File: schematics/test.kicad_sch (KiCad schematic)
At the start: 9 parts, among them J1 Conn_01x03_Pin, J3 Conn_01x03_Pin, J4 GY-91 MPU6500 + BMP280, Q1 2N2222

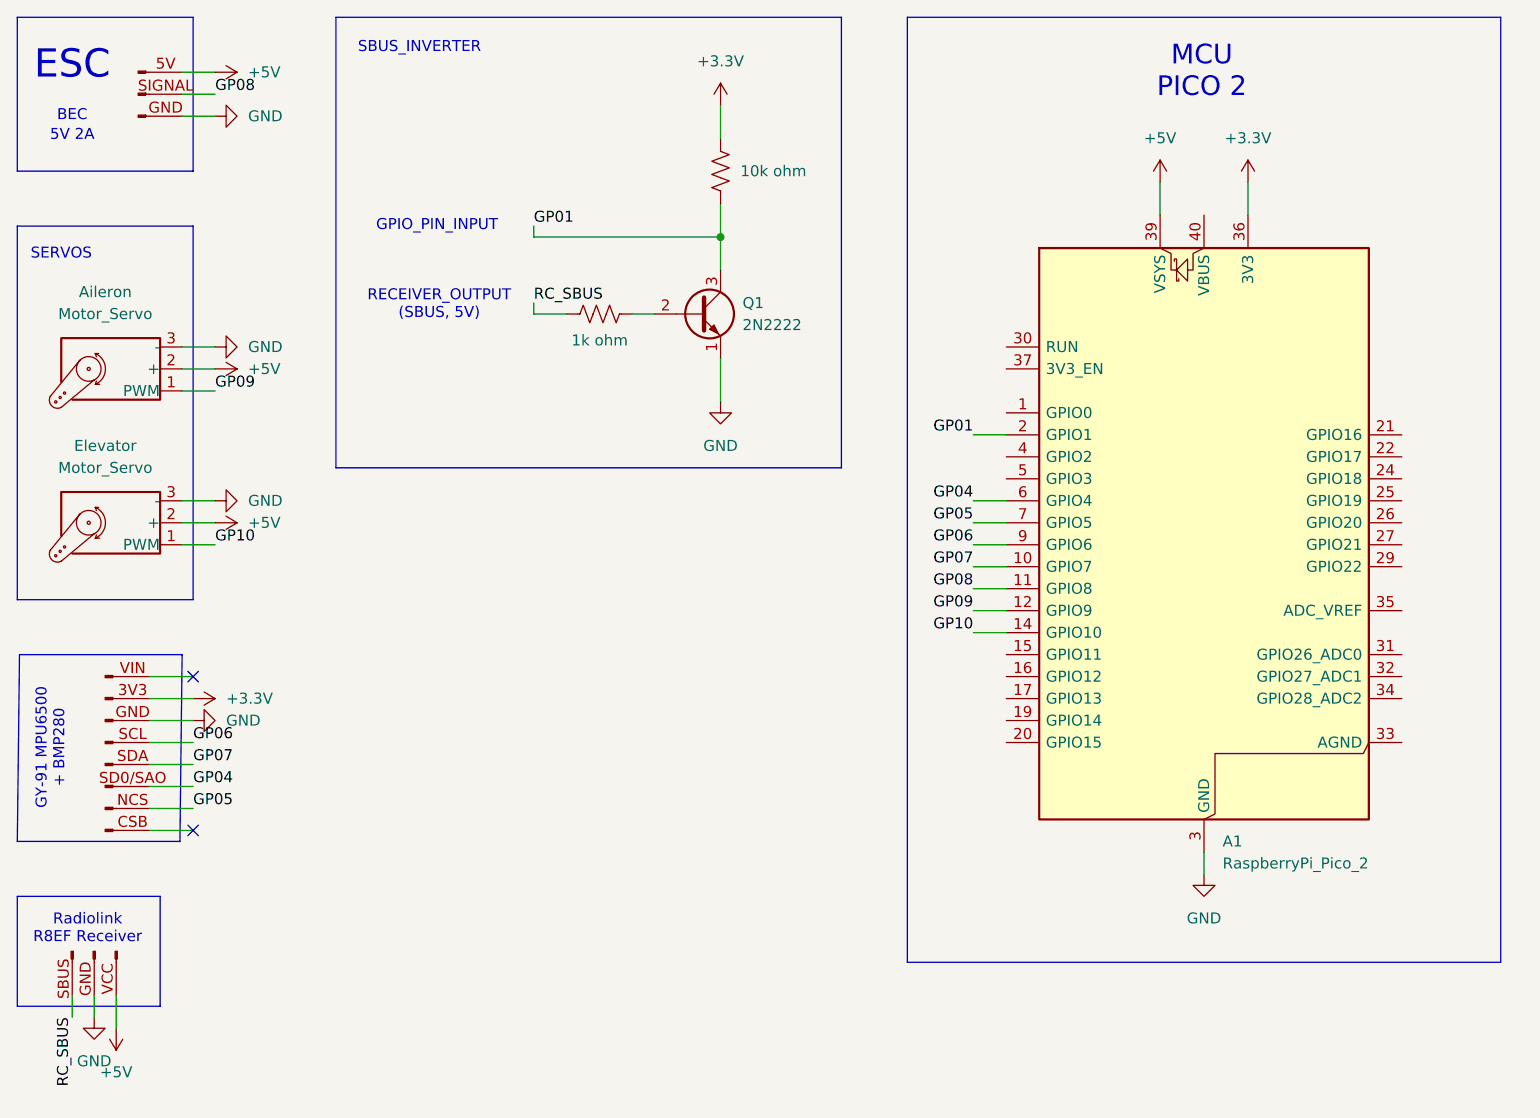
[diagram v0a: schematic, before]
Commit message: schematic, bom updates
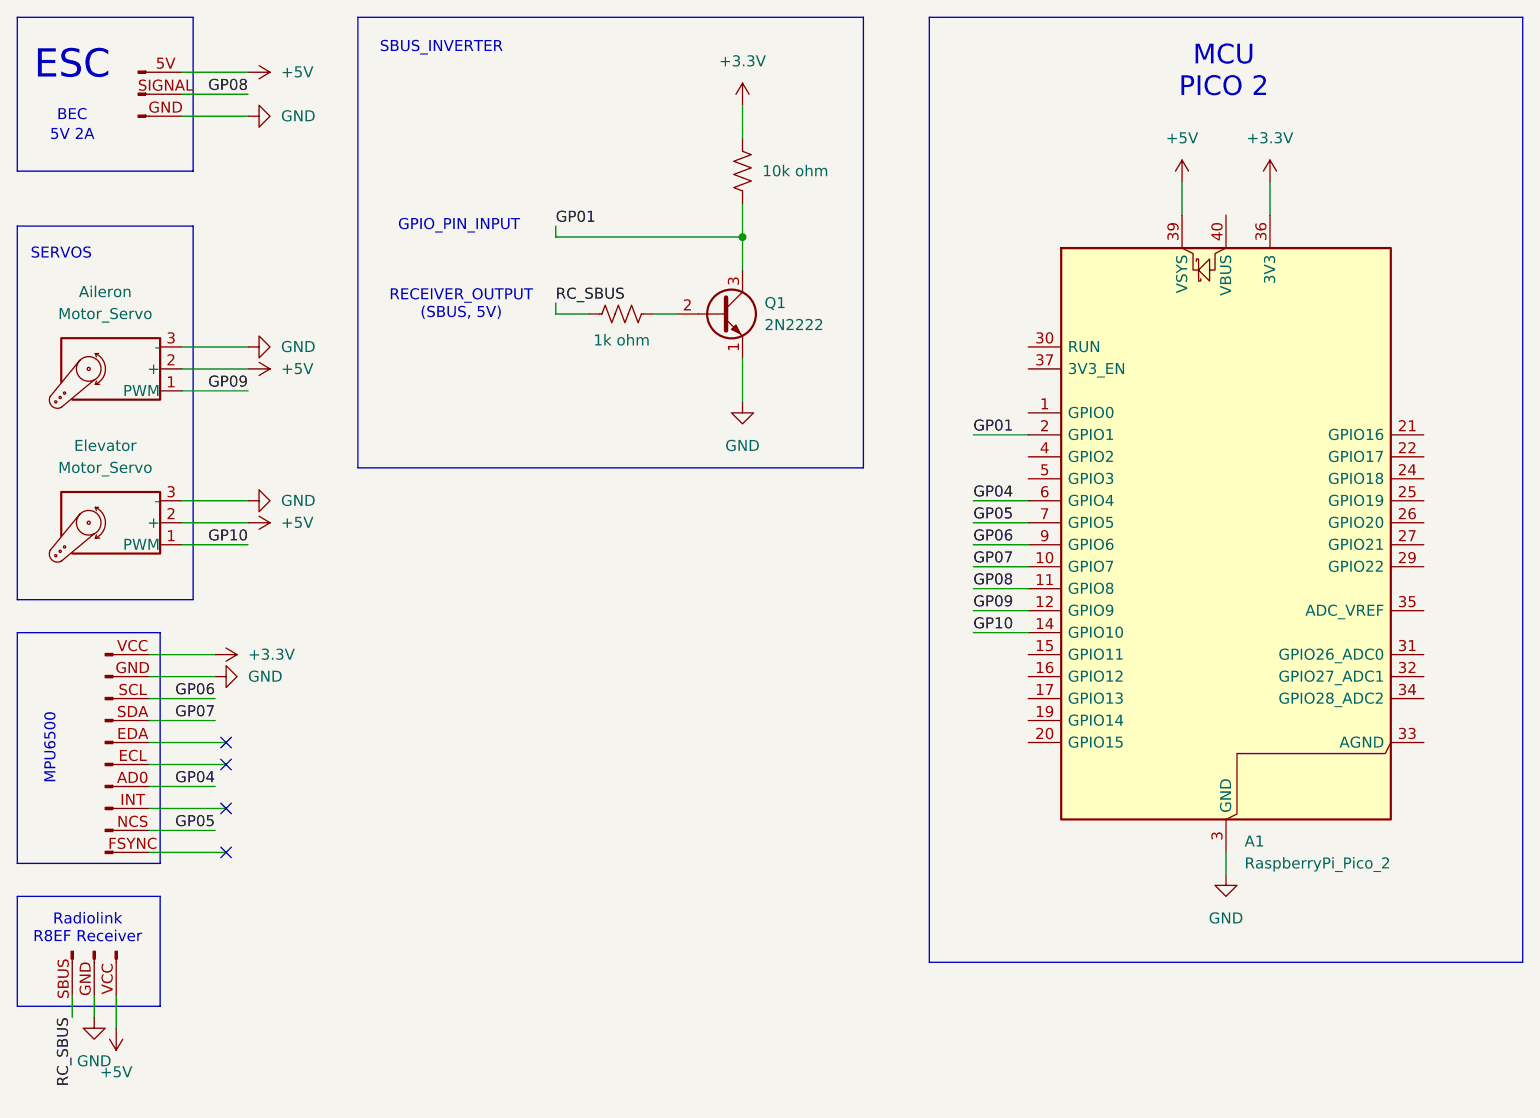
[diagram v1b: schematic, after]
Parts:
- J4: symbol Connector:Conn_01x08_Pin -> Connector:Conn_01x10_Pin
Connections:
- net +3.3V: now also J4.VCC (Pin_1); no longer J4.3V3 (Pin_2)
- net GP04: now also J4.AD0 (Pin_7); no longer J4.SD0/SAO (Pin_6)
- no-connect marks 2 -> 4
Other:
- note added: "MPU6500"
- note removed: "GY-91 MPU6500 + BMP280"
- moved on the sheet: A1, Q1
